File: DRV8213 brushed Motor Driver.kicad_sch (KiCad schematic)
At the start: 27 parts, among them J1 Keystone 6102, J10 Precidip 852-10-004-20-001101, J11 Precidip 852-10-004-20-001101, J2 Keystone 6102, J3 Keystone 6100, J4 Keystone 6100, J5 Keystone 6102, J6 Keystone 6102, J7 Keystone 6100, J8 Keystone 6100, J9 JST PH 2mm horizontal, U1 DRV8213RTER, U2 LP2981-3.3

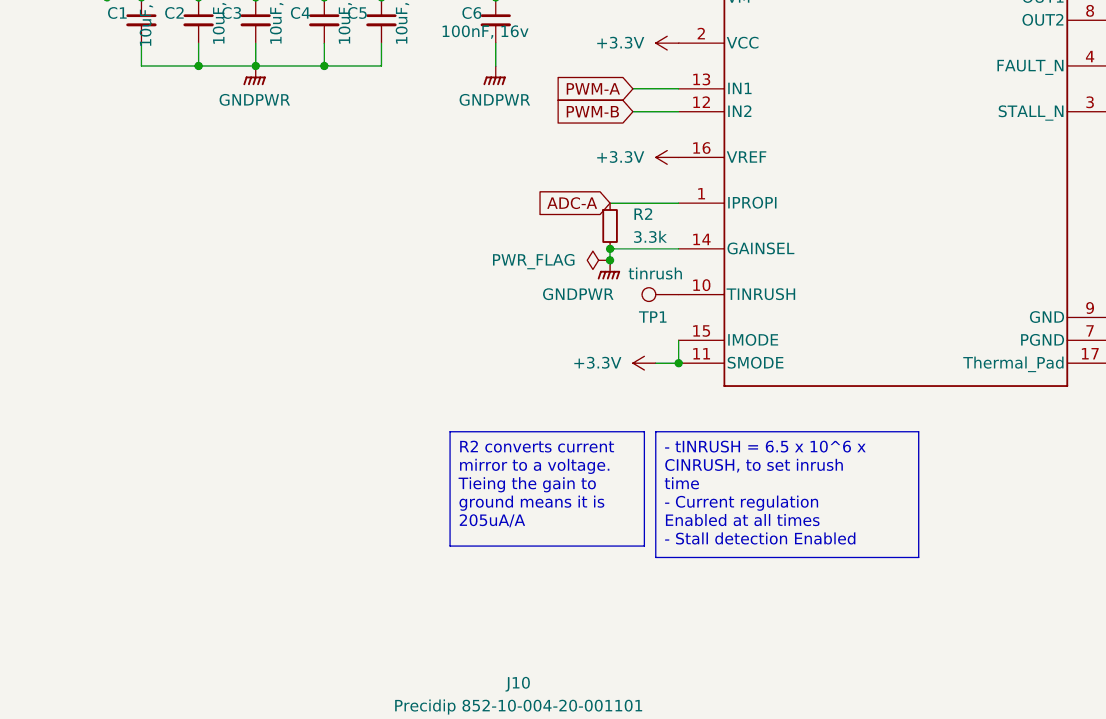
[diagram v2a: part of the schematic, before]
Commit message: Added inrush current blank capacitor
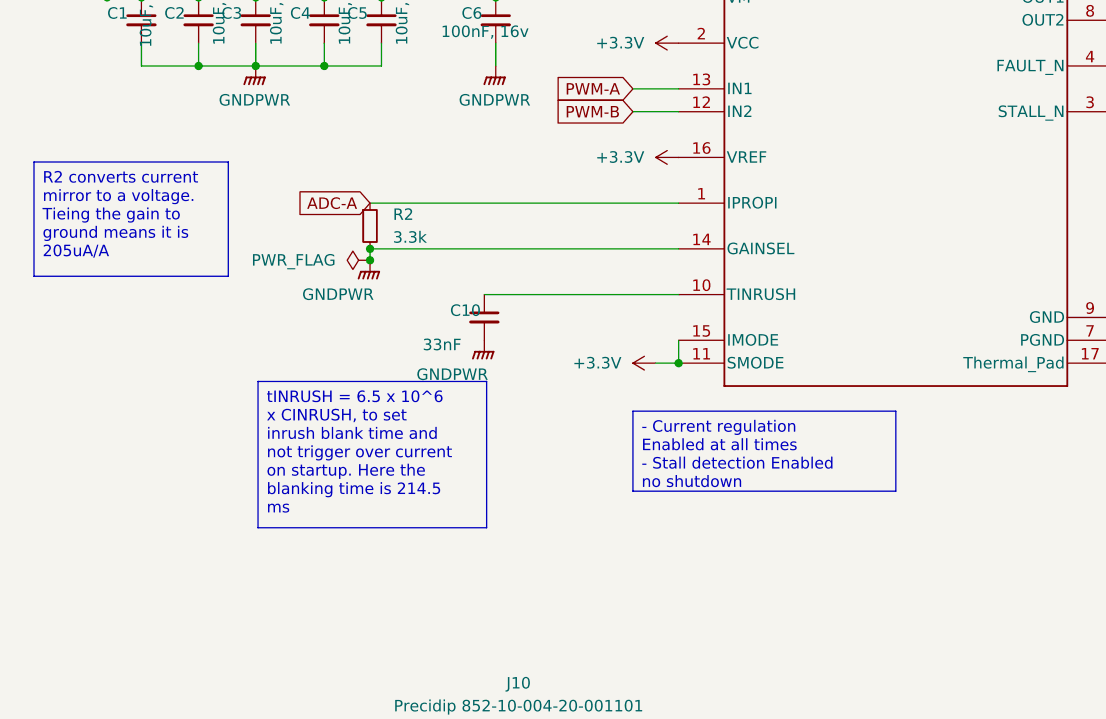
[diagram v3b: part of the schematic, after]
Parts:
- removed TP1: tinrush, TestPoint:TestPoint_Pad_D1.0mm, symbol Connector:TestPoint
- added C10: 33nF, Capacitor_SMD:C_0603_1608Metric, symbol Device:C_Small
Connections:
- net GNDPWR: now also C10.2
- net at U1.10 (TINRUSH): now also C10.1
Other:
- moved on the sheet: R2
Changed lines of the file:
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@@
 	(text_box "R2 converts current mirror to a voltage. Tieing the gain to ground means it is 205uA/A"
 		(exclude_from_sim no)
-		(at 62.23 107.95 0)
+		(at 16.002 77.978 0)
 		(size 21.59 12.7)
 		(margins 0.9525 0.9525 0.9525 0.9525)
@@
 		)
 	)
-	(text_box "- tINRUSH = 6.5 x 10^6 x CINRUSH, to set inrush time\n- Current regulation Enabled at all times\n- Stall detection Enabled"
+	(text_box "- Current regulation Enabled at all times\n- Stall detection Enabled no shutdown"
 		(exclude_from_sim no)
-		(at 85.09 107.95 0)
-		(size 29.21 13.97)
+		(at 82.55 105.664 0)
+		(size 29.21 8.89)
 		(margins 0.9525 0.9525 0.9525 0.9525)
 		(stroke
 			(width 0)
-			(type default)
+			(type solid)
 		)
 		(fill
@@
 		)
 	)
+	(text_box "tINRUSH = 6.5 x 10^6 x CINRUSH, to set inrush blank time and not trigger over current on startup. Here the blanking time is 214.5 ms"
+		(exclude_from_sim no)
+		(at 40.894 102.362 0)
+		(size 25.4 16.256)
+		(margins 0.9525 0.9525 0.9525 0.9525)
+		(stroke
+			(width 0)
+			(type solid)
+		)
+		(fill
+			(type none)
+		)
+		(effects
+			(font
+				(size 1.27 1.27)
+			)
+			(justify left top)
+		)
+	)
 	(junction
 		(at 48.26 59.69)
@@
 	)
 	(junction
-		(at 80.01 87.63)
+		(at 53.34 87.63)
 		(diameter 0)
 		(color 0 0 0 0)
@@
 	)
 	(junction
-		(at 80.01 88.9)
+		(at 53.34 88.9)
 		(diameter 0)
 		(color 0 0 0 0)
@@
 	(wire
 		(pts
-			(xy 80.01 82.55) (xy 87.63 82.55)
+			(xy 53.34 82.55) (xy 87.63 82.55)
 		)
 		(stroke
@@
 	(wire
 		(pts
-			(xy 87.63 87.63) (xy 80.01 87.63)
+			(xy 53.34 87.63) (xy 87.63 87.63)
 		)
 		(stroke
@@
 	(wire
 		(pts
+			(xy 66.04 92.71) (xy 87.63 92.71)
+		)
+		(stroke
+			(width 0)
+			(type default)
+		)
+	)
+	(wire
+		(pts
 			(xy 59.69 142.24) (xy 63.5 142.24)
 		)
@@
 	(wire
 		(pts
-			(xy 80.01 87.63) (xy 80.01 88.9)
+			(xy 53.34 87.63) (xy 53.34 88.9)
 		)
 		(stroke
@@
 	(global_label "ADC-A"
 		(shape input)
-		(at 80.01 82.55 180)
+		(at 53.34 82.55 180)
 		(fields_autoplaced yes)
 		(effects
@@
 		)
 		(property "Intersheetrefs" "${INTERSHEET_REFS}"
-			(at 70.7352 82.55 0)
+			(at 44.0652 82.55 0)
 			(effects
 				(font
@@
 	)
 	(symbol
+		(lib_id "Device:C_Small")
+		(at 66.04 95.25 0)
+		(unit 1)
+		(exclude_from_sim no)
+		(in_bom yes)
+		(on_board yes)
+		(dnp no)
+		(property "Reference" "C10"
+			(at 62.23 94.488 0)
+			(effects
+				(font
+					(size 1.27 1.27)
+				)
+				(justify left)
+			)
+		)
+		(property "Value" "33nF"
+			(at 59.182 98.298 0)
+			(effects
+				(font
+					(size 1.27 1.27)
+				)
+				(justify left)
+			)
+		)
+		(property "Footprint" "Capacitor_SMD:C_0603_1608Metric"
+			(at 66.04 95.25 0)
+			(effects
+				(font
+					(size 1.27 1.27)
+				)
+				(hide yes)
+			)
+		)
+		(property "Datasheet" "~"
+			(at 66.04 95.25 0)
+			(effects
+				(font
+					(size 1.27 1.27)
+				)
+				(hide yes)
+			)
+		)
+		(property "Description" "Unpolarized capacitor, small symbol"
+			(at 66.04 95.25 0)
+			(effects
+				(font
+					(size 1.27 1.27)
+				)
+				(hide yes)
+			)
+		)
+		(property "LCSC" "C21117"
+			(at 62.23 94.488 0)
+			(effects
+				(font
+					(size 1.27 1.27)
+				)
+				(hide yes)
+			)
+		)
+		(pin "1"
+		)
+		(pin "2"
+		)
+		(instances
+			(project "DRV8213 brushed Motor Driver"
+				(path "/8760dbe3-976e-4366-afd9-aec15b99495c"
+					(reference "C10")
+					(unit 1)
+				)
+			)
+		)
+	)
+	(symbol
 		(lib_id "power:+3.3V")
 		(at 87.63 64.77 90)
@@
 	(symbol
 		(lib_id "Device:R_Small")
-		(at 80.01 85.09 0)
+		(at 53.34 85.09 0)
 		(unit 1)
 		(exclude_from_sim no)
@@
 		(fields_autoplaced yes)
 		(property "Reference" "R2"
-			(at 82.55 83.8199 0)
+			(at 55.88 83.8199 0)
 			(effects
 				(font
@@
 		)
 		(property "Value" "3.3k"
-			(at 82.55 86.3599 0)
+			(at 55.88 86.3599 0)
 			(effects
 				(font
@@
 		)
 		(property "Footprint" "Resistor_SMD:R_0402_1005Metric"
-			(at 80.01 85.09 0)
+			(at 53.34 85.09 0)
 			(effects
 				(font
@@
 		)
 		(property "Datasheet" "~"
-			(at 80.01 85.09 0)
+			(at 53.34 85.09 0)
 			(effects
 				(font
@@
 		)
 		(property "Description" "Resistor, small symbol"
-			(at 80.01 85.09 0)
+			(at 53.34 85.09 0)
 			(effects
 				(font
@@
 		)
 		(property "LCSC" "C25890"
-			(at 82.55 83.8199 0)
+			(at 55.88 83.8199 0)
 			(effects
 				(font
@@
 	)
 	(symbol
+		(lib_id "power:GNDPWR")
+		(at 66.04 97.79 0)
+		(unit 1)
+		(exclude_from_sim no)
+		(in_bom yes)
+		(on_board yes)
+		(dnp no)
+		(property "Reference" "#PWR019"
+			(at 66.04 102.87 0)
+			(effects
+				(font
+					(size 1.27 1.27)
+				)
+				(hide yes)
+			)
+		)
+		(property "Value" "GNDPWR"
+			(at 62.484 101.6 0)
+			(effects
+				(font
+					(size 1.27 1.27)
+				)
+			)
+		)
+		(property "Footprint" ""
+			(at 66.04 99.06 0)
+			(effects
+				(font
+					(size 1.27 1.27)
+				)
+				(hide yes)
+			)
+		)
+		(property "Datasheet" ""
+			(at 66.04 99.06 0)
+			(effects
+				(font
+					(size 1.27 1.27)
+				)
+				(hide yes)
+			)
+		)
+		(property "Description" "Power symbol creates a global label with name \"GNDPWR\" , global ground"
+			(at 66.04 97.79 0)
+			(effects
+				(font
+					(size 1.27 1.27)
+				)
+				(hide yes)
+			)
+		)
+		(pin "1"
+		)
+		(instances
+			(project "DRV8213 brushed Motor Driver"
+				(path "/8760dbe3-976e-4366-afd9-aec15b99495c"
+					(reference "#PWR019")
+					(unit 1)
+				)
+			)
+		)
+	)
+	(symbol
 		(lib_id "Device:C_Small")
 		(at 252.73 125.73 0)
@@
 	(symbol
 		(lib_id "power:PWR_FLAG")
-		(at 80.01 88.9 90)
+		(at 53.34 88.9 90)
 		(unit 1)
 		(exclude_from_sim no)
@@
 		(fields_autoplaced yes)
 		(property "Reference" "#FLG02"
-			(at 78.105 88.9 0)
+			(at 51.435 88.9 0)
 			(effects
 				(font
@@
 		)
 		(property "Value" "PWR_FLAG"
-			(at 76.2 88.8999 90)
+			(at 49.53 88.8999 90)
 			(effects
 				(font
@@
 		)
 		(property "Footprint" ""
-			(at 80.01 88.9 0)
+			(at 53.34 88.9 0)
 			(effects
 				(font
@@
 		)
 		(property "Datasheet" "~"
-			(at 80.01 88.9 0)
+			(at 53.34 88.9 0)
 			(effects
 				(font
@@
 		)
 		(property "Description" "Special symbol for telling ERC where power comes from"
-			(at 80.01 88.9 0)
+			(at 53.34 88.9 0)
 			(effects
 				(font
@@
 	(symbol
 		(lib_id "power:GNDPWR")
-		(at 80.01 88.9 0)
+		(at 53.34 88.9 0)
 		(unit 1)
 		(exclude_from_sim no)
@@
 		(dnp no)
 		(property "Reference" "#PWR012"
-			(at 80.01 93.98 0)
+			(at 53.34 93.98 0)
 			(effects
 				(font
@@
 		)
 		(property "Value" "GNDPWR"
-			(at 76.454 92.71 0)
+			(at 49.784 92.71 0)
 			(effects
 				(font
@@
 		)
 		(property "Footprint" ""
-			(at 80.01 90.17 0)
+			(at 53.34 90.17 0)
 			(effects
 				(font
@@
 		)
 		(property "Datasheet" ""
-			(at 80.01 90.17 0)
+			(at 53.34 90.17 0)
 			(effects
 				(font
@@
 		)
 		(property "Description" "Power symbol creates a global label with name \"GNDPWR\" , global ground"
-			(at 80.01 88.9 0)
+			(at 53.34 88.9 0)
 			(effects
 				(font
@@
 					(unit 1)
 				)
-			)
-		)
-	)
-	(symbol
-		(lib_id "Connector:TestPoint")
-		(at 87.63 92.71 90)
-		(unit 1)
-		(exclude_from_sim no)
-		(in_bom no)
-		(on_board yes)
-		(dnp no)
-		(property "Reference" "TP1"
-			(at 84.836 95.25 90)
-			(effects
-				(font
-					(size 1.27 1.27)
-				)
-			)
-		)
-		(property "Value" "tinrush"
-			(at 85.09 90.424 90)
-			(effects
-				(font
-					(size 1.27 1.27)
-				)
-			)
-		)
-		(property "Footprint" "TestPoint:TestPoint_Pad_D1.0mm"
-			(at 87.63 87.63 0)
-			(effects
-				(font
-					(size 1.27 1.27)
-				)
-				(hide yes)
-			)
-		)
-		(property "Datasheet" "~"
-			(at 87.63 87.63 0)
-			(effects
-				(font
-					(size 1.27 1.27)
-				)
-				(hide yes)
-			)
-		)
-		(property "Description" "test point"
-			(at 87.63 92.71 0)
-			(effects
-				(font
-					(size 1.27 1.27)
-				)
-				(hide yes)
-			)
-		)
-		(pin "1"
-		)
-		(instances
-			(project "DRV8213 brushed Motor Driver"
-				(path "/8760dbe3-976e-4366-afd9-aec15b99495c"
-					(reference "TP1")
-					(unit 1)
-				)

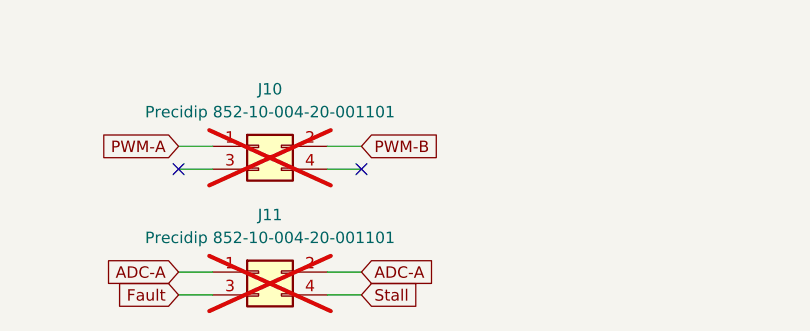
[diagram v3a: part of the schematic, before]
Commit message: Update ADC pin assignment
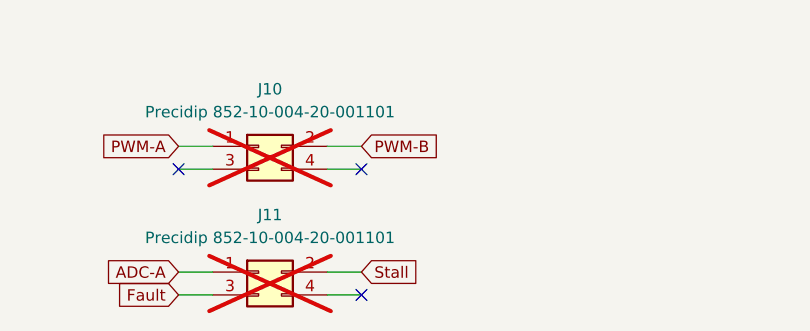
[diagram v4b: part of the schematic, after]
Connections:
- net ADC-A: no longer J11.2 (Pin_2)
- net Stall: now also J11.2 (Pin_2); no longer J11.4 (Pin_4)
- no-connect marks 3 -> 4
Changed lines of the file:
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@@
+	)
+	(no_connect
+		(at 80.01 158.75)
 	)
 	(no_connect
@@
 			(width 0)
 			(type default)
-		)
-	)
-	(global_label "ADC-A"
-		(shape input)
-		(at 80.01 156.21 0)
-		(fields_autoplaced yes)
-		(effects
-			(font
-				(size 1.27 1.27)
-			)
-			(justify left)
-		)
-		(property "Intersheetrefs" "${INTERSHEET_REFS}"
-			(at 89.2848 156.21 0)
-			(effects
-				(font
-					(size 1.27 1.27)
-				)
-				(justify left)
-				(hide yes)
-			)
 		)
 	)
@@
 	(global_label "Stall"
 		(shape input)
-		(at 80.01 158.75 0)
+		(at 80.01 156.21 0)
 		(fields_autoplaced yes)
 		(effects
@@
 		)
 		(property "Intersheetrefs" "${INTERSHEET_REFS}"
-			(at 87.4098 158.75 0)
+			(at 87.4098 156.21 0)
 			(effects
 				(font

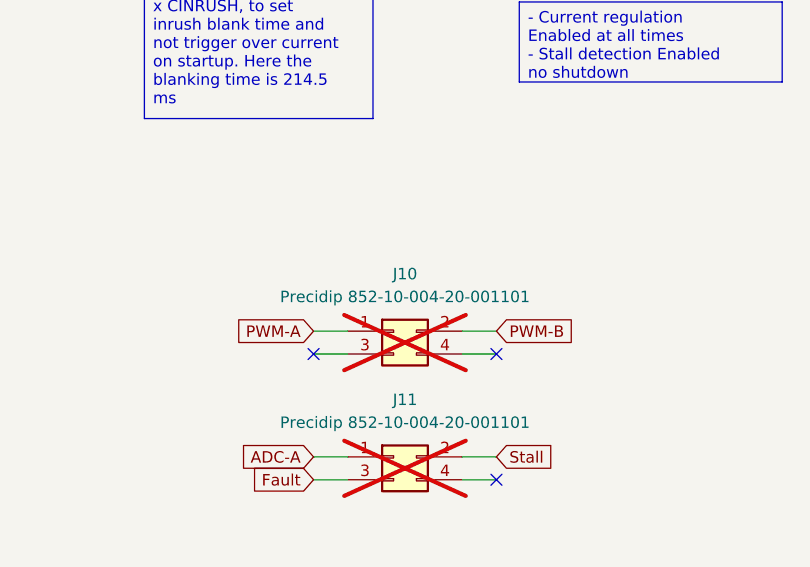
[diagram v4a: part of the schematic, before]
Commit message: Reversed connector pin assignments to mirror hub
Technically any pin would work, but I want it logical order with A matching with A. Some hubs may not have enough pins also, so most important pins go first. I might change the footprint numbers to match as well, but this is less important.
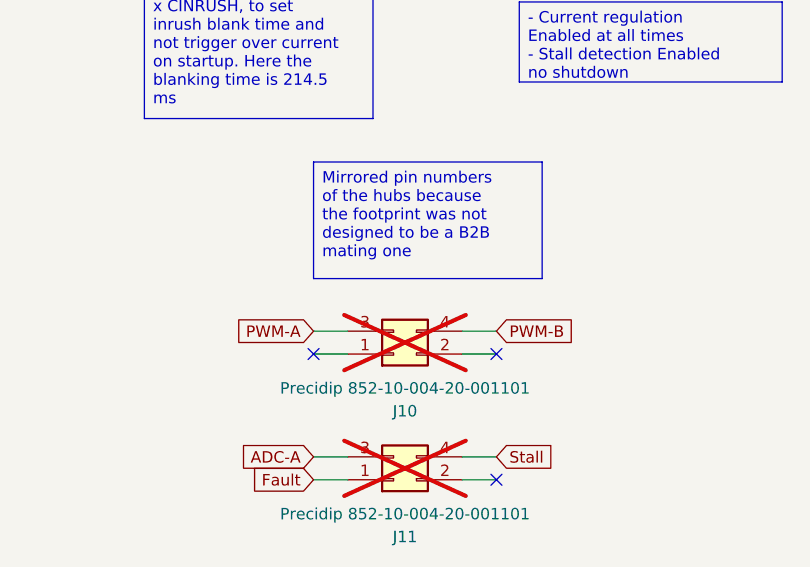
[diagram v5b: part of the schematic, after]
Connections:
- net ADC-A: now also J11.3 (Pin_3); no longer J11.1 (Pin_1)
- net Fault: now also J11.1 (Pin_1); no longer J11.3 (Pin_3)
- net PWM-A: now also J10.3 (Pin_3); no longer J10.1 (Pin_1)
- net PWM-B: now also J10.4 (Pin_4); no longer J10.2 (Pin_2)
- net Stall: now also J11.4 (Pin_4); no longer J11.2 (Pin_2)
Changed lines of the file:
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@@
+		)
+	)
+	(text_box "Mirrored pin numbers of the hubs because the footprint was not designed to be a B2B mating one"
+		(exclude_from_sim no)
+		(at 59.69 123.444 0)
+		(size 25.4 12.954)
+		(margins 0.9525 0.9525 0.9525 0.9525)
+		(stroke
+			(width 0)
+			(type solid)
+		)
+		(fill
+			(type none)
+		)
+		(effects
+			(font
+				(size 1.27 1.27)
+			)
+			(justify left top)
 		)
 	)
@@
 	(symbol
 		(lib_id "Connector_Generic:Conn_02x02_Odd_Even")
-		(at 68.58 156.21 0)
+		(at 68.58 158.75 0)
+		(mirror x)
 		(unit 1)
 		(exclude_from_sim no)
@@
 		(on_board yes)
 		(dnp yes)
-		(fields_autoplaced yes)
 		(property "Reference" "J11"
-			(at 69.85 149.86 0)
+			(at 69.85 165.1 0)
 			(effects
 				(font
@@
 		)
 		(property "Value" "Precidip 852-10-004-20-001101"
-			(at 69.85 152.4 0)
+			(at 69.85 162.56 0)
 			(effects
 				(font
@@
 		)
 		(property "Footprint" "custom_Connector:Precidip 852-10-004-20-001101"
-			(at 68.58 156.21 0)
+			(at 68.58 158.75 0)
 			(effects
 				(font
@@
 		)
 		(property "Datasheet" "~"
-			(at 68.58 156.21 0)
+			(at 68.58 158.75 0)
 			(effects
 				(font
@@
 		)
 		(property "Description" "Generic connector, double row, 02x02, odd/even pin numbering scheme (row 1 odd numbers, row 2 even numbers), script generated (kicad-library-utils/schlib/autogen/connector/)"
-			(at 68.58 156.21 0)
+			(at 68.58 158.75 0)
 			(effects
 				(font
@@
 	(symbol
 		(lib_id "Connector_Generic:Conn_02x02_Odd_Even")
-		(at 68.58 142.24 0)
+		(at 68.58 144.78 0)
+		(mirror x)
 		(unit 1)
 		(exclude_from_sim no)
@@
 		(on_board yes)
 		(dnp yes)
-		(fields_autoplaced yes)
 		(property "Reference" "J10"
-			(at 69.85 135.89 0)
+			(at 69.85 151.13 0)
 			(effects
 				(font
@@
 		)
 		(property "Value" "Precidip 852-10-004-20-001101"
-			(at 69.85 138.43 0)
+			(at 69.85 148.59 0)
 			(effects
 				(font
@@
 		)
 		(property "Footprint" "custom_Connector:Precidip 852-10-004-20-001101"
-			(at 68.58 142.24 0)
+			(at 68.58 144.78 0)
 			(effects
 				(font
@@
 		)
 		(property "Datasheet" "~"
-			(at 68.58 142.24 0)
+			(at 68.58 144.78 0)
 			(effects
 				(font
@@
 		)
 		(property "Description" "Generic connector, double row, 02x02, odd/even pin numbering scheme (row 1 odd numbers, row 2 even numbers), script generated (kicad-library-utils/schlib/autogen/connector/)"
-			(at 68.58 142.24 0)
-			(effects
-				(font
+			(at 68.58 144.78 0)
+			(effects
+				(font
